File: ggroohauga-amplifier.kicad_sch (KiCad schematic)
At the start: 0 parts

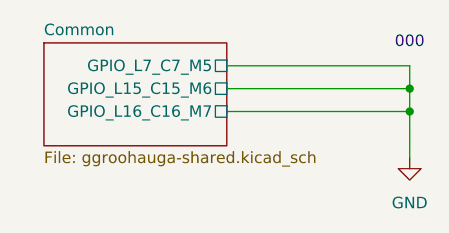
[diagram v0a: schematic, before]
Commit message: Add "BOARD_ID" to the GPIOs for that and fix net names on unused GPIOs
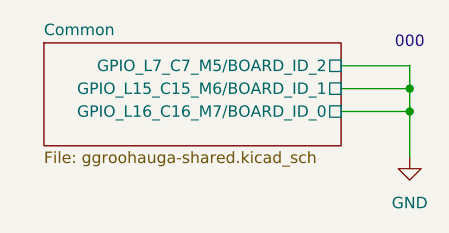
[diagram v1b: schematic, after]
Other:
- sheet Common ports: added GPIO_L15_C15_M6/BOARD_ID_1, GPIO_L16_C16_M7/BOARD_ID_0, GPIO_L7_C7_M5/BOARD_ID_2; removed GPIO_L15_C15_M6, GPIO_L16_C16_M7, GPIO_L7_C7_M5
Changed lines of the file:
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@@
 	(wire
 		(pts
-			(xy 58.42 21.59) (xy 58.42 24.13)
+			(xy 50.8 26.67) (xy 58.42 26.67)
 		)
 		(stroke
@@
 	(wire
 		(pts
-			(xy 38.1 21.59) (xy 58.42 21.59)
+			(xy 50.8 24.13) (xy 58.42 24.13)
+		)
+		(stroke
+			(width 0)
+			(type default)
+		)
+	)
+	(wire
+		(pts
+			(xy 58.42 26.67) (xy 58.42 31.75)
+		)
+		(stroke
+			(width 0)
+			(type default)
+		)
+	)
+	(wire
+		(pts
+			(xy 58.42 21.59) (xy 58.42 24.13)
 		)
 		(stroke
@@
 	(wire
 		(pts
-			(xy 58.42 26.67) (xy 58.42 31.75)
-		)
-		(stroke
-			(width 0)
-			(type default)
-		)
-	)
-	(wire
-		(pts
-			(xy 38.1 26.67) (xy 58.42 26.67)
-		)
-		(stroke
-			(width 0)
-			(type default)
-		)
-	)
-	(wire
-		(pts
-			(xy 38.1 24.13) (xy 58.42 24.13)
+			(xy 50.8 21.59) (xy 58.42 21.59)
 		)
 		(stroke
@@
 	(sheet
 		(at 17.78 19.05)
-		(size 20.32 11.43)
+		(size 33.02 11.43)
 		(exclude_from_sim no)
 		(in_bom yes)
@@
 			)
 		)
-		(pin "GPIO_L7_C7_M5" passive
-			(at 38.1 21.59 0)
+		(pin "GPIO_L7_C7_M5{slash}BOARD_ID_2" passive
+			(at 50.8 21.59 0)
 			(effects
 				(font
@@
 			)
 		)
-		(pin "GPIO_L15_C15_M6" passive
-			(at 38.1 24.13 0)
+		(pin "GPIO_L15_C15_M6{slash}BOARD_ID_1" passive
+			(at 50.8 24.13 0)
 			(effects
 				(font
@@
 			)
 		)
-		(pin "GPIO_L16_C16_M7" passive
-			(at 38.1 26.67 0)
+		(pin "GPIO_L16_C16_M7{slash}BOARD_ID_0" passive
+			(at 50.8 26.67 0)
 			(effects
 				(font
